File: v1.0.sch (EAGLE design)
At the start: 264 parts, among them J1 DC-044-A, J2 MICROSD-9P, J3 2p-2.54, J4 2p-2.54, J5 16p-2.54, J6 16p-2.54, J8 2p-2.54, Q2 SSM3J328R,LF, Q3 6pF@32.7680kHz, Q4 BSS138W-7-F, Q5 SSM3J328R,LF, SW1 TS-1101F, SW2 TS-1101F, SW3 TS-1101F, SW4 TS-1101F, SW5 TS-1101F, U1 MCP23017-E/SO, U10 74HC139N, U11 BZX84C30, U12 SP483ECN-L, U13 FT232RL-SSOP28, U14 FT232RL-SSOP28, U15 FT232RL-SSOP28, U2 MCP79412-I/SN, U3 LOPY, U4 MAX213IDBR, U5 FT232RL-SSOP28, U6 FT232RL-SSOP28, U7 2x14p-2.54, U8 BR24G32-3, U9 2x14p-2.54, Y2 12MHZ

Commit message: General pendantry of tidying and ERC etc
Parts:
- removed C33: 10uf, Seeed-Capacitor-2016:CERAMIC-10UF-25V-10%-X5R(0805)
- added C26: 10uf, Seeed-Capacitor:TANTALUM-SMD-10UF-16V-10%(AVX-A)
- added D22: RED-0603, Seeed-LED-2016:LED-SMD-RED-DIFFUSED(0603)
- added R4: 220R, Seeed-Resistor:SMD-RES-220R-5%-1/10W(0603)
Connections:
- net LOPY_I2C_5V_PROTECTED renamed N$4
- net PI_I2C_2_5V_P renamed PI_I2C_5V_P2
- net PI_I2C_3V3_10_P renamed PI_I2C_3V3_10
- net PI_I2C_3V3_2_P renamed PI_I2C_3V3_2
- net PI_I2C_3V3_3_P renamed PI_I2C_3V3_1
- net PI_I2C_3V3_4_P renamed PI_I2C_3V3_4
- net PI_I2C_5V_10_P renamed PI_I2C_5V_P9
- net PI_I2C_5V_3_P renamed PI_I2C_5V_P1
- net PI_I2C_5V_4_P renamed PI_I2C_5V_P3
- removed net +3V3_PP: F62.1
- removed net N$18: J2.DATA2
- removed net N$20: J2.DATA1
- removed net N$21: J2.CDN
- removed net PI_I2C_3V3_5_P: F14.2, I2C_6-2.S
- removed net PI_I2C_3V3_6_P: F22.2, I2C_5-2.S
- removed net PI_I2C_3V3_7_P: F16.2, I2C_7-2.S
- removed net PI_I2C_3V3_8_P: F18.2, I2C_8-2.S
- removed net PI_I2C_3V3_9_P: F20.2, I2C_9-2.S
- removed net PI_I2C_5V_5_P: F13.2, I2C_6-1.S
- removed net PI_I2C_5V_6_P: F21.2, I2C_5-1.S
- removed net PI_I2C_5V_7_P: F15.2, I2C_7-1.S
- removed net PI_I2C_5V_8_P: F17.2, I2C_8-1.S
- removed net PI_I2C_5V_9_P: F19.2, I2C_9-1.S
- new net N$5: D22.+, R4.1
- new net PI_I2C_3V3_5: F14.2, I2C_5-2.S
- new net PI_I2C_3V3_6: F16.2, I2C_6-2.S
- new net PI_I2C_3V3_7: F18.2, I2C_7-2.S
- new net PI_I2C_3V3_8: F20.2, I2C_8-2.S
- new net PI_I2C_3V3_9: F22.2, I2C_9-2.S
- new net PI_I2C_5V_P4: F13.2, I2C_5-1.S
- new net PI_I2C_5V_P5: F15.2, I2C_6-1.S
- new net PI_I2C_5V_P6: F17.2, I2C_7-1.S
- new net PI_I2C_5V_P7: F19.2, I2C_8-1.S
- new net PI_I2C_5V_P8: F21.2, I2C_9-1.S
- net +3V3: now also F62.1
- net GND: now also C17.-, C25.1, C26.-, USB1.GND, USB1.SHIELD; no longer C17.+, C33.1
- net LOPY_USB_5V: now also C17.+; no longer C17.-
- net N$105: now also C26.+; no longer C33.2
- net N$83: now also D22.-
- net PI_PWR_CTRL: now also R4.2
- net RXD1: now also U4.ROUT1; no longer U4.DIN1
- net RXD2: now also U4.ROUT2; no longer U4.DIN2
- net RXD3: now also U4.ROUT3; no longer U4.DIN3
- net SHIELD: no longer C25.1, USB1.GND, USB1.SHIELD
- net TXD1: now also U4.DIN1; no longer U4.ROUT1
- net TXD2: now also U4.DIN2; no longer U4.ROUT2
- net TXD3: now also U4.DIN3; no longer U4.ROUT3
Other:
- note added: "Bootloader pins"
- note added: "I2C Sockets"
- note added: "LoPy I2C"
- note added: "LoPy UART"
- note added: "Needs good ground plane for termal issues"
- note added: "RS232"
- note added: "SPI Sockets"
- note added: "TP4 & TP1 should be close together"
- note added: "TTL"
- note added: "crystal tracks should be symetrical"
- note removed: "RPI HUB UART"
- note removed: "RS485 Rpi"
- note removed: "lopy I2C"
- note removed: "lopy SPI"
- note removed: "lopy UART"
- moved on the sheet: BAT1, C13, C17, C19, C20, C23, C25, C28, C30, C32, C34, C35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

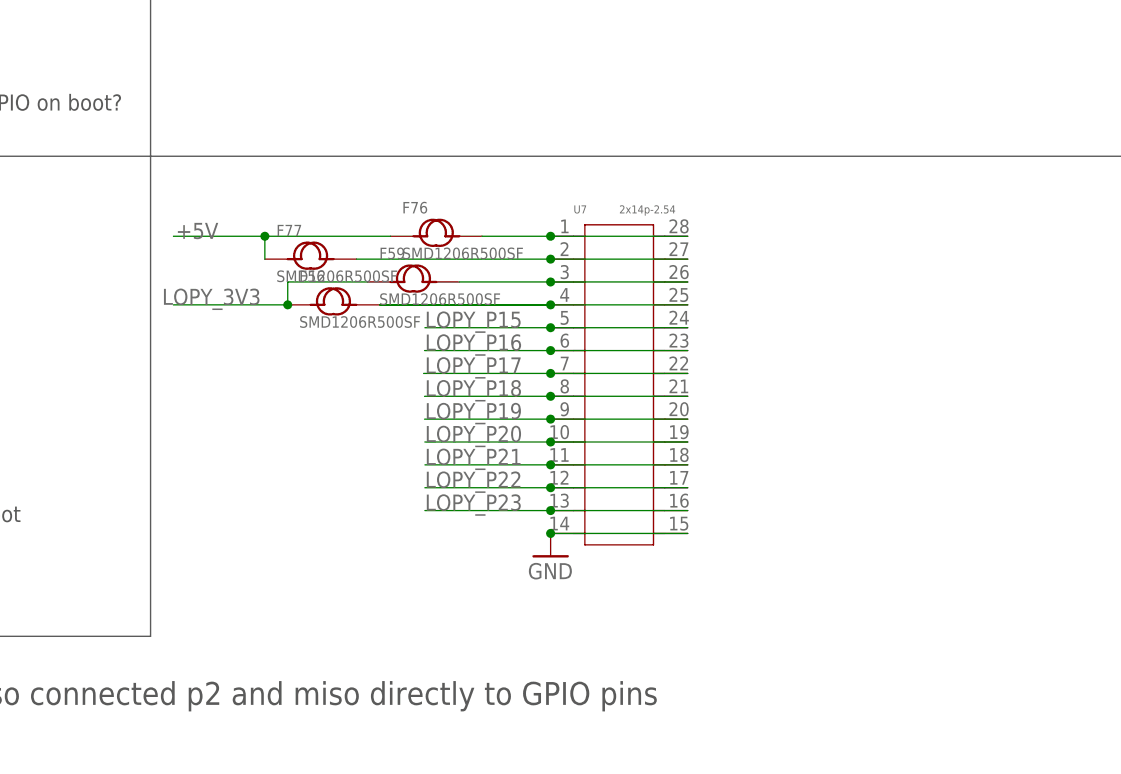
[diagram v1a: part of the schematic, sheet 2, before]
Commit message: Clustering things ready for PCB layout
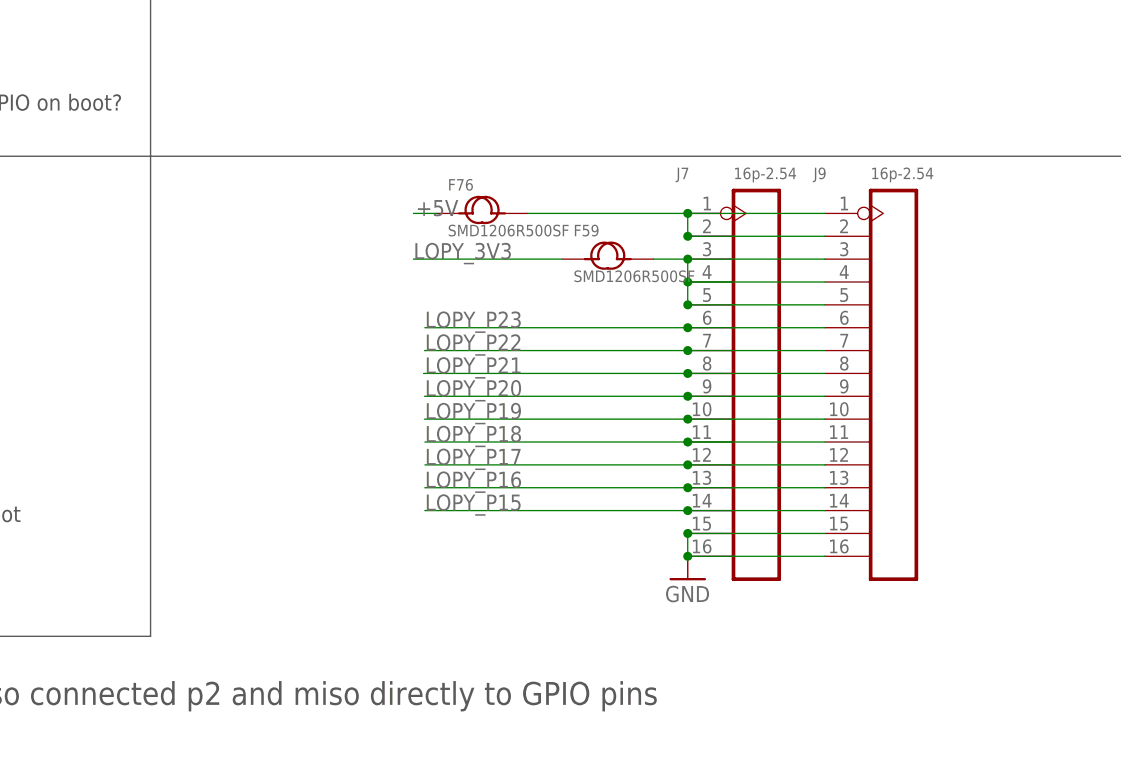
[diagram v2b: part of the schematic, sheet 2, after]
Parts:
- removed F56, F61, F63, F77: SMD1206R500SF, Seeed-Fuse:SMD-PPTC-500MA(1206)
- removed SW4: TS-1101F, Seeed-Switch-2016:DIP-BUTTON(2P-6.0X3.0X4.3MM)-TS-1101F
- removed U7, U9: 2x14p-2.54, Seeed-Connector:DIP-IC-SOCKET(2X14P-2.54)
- added J10, J11, J7, J9: 16p-2.54, Seeed-Connector:DIP-BLACK-MALE-HEADER-VERT(16P-2.54)
- added TP16: TPB2,54, testpad:TPB2,54
- Q1: value 6pF@32.7680kHz -> 32.768khZ@6Pf
- U10: value 74HC139N -> 74HCT139D; device 74HC139N:74HC139N -> imported-parts:74HCT139D
- renumbered Q3 to Q1
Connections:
- net N$12 renamed GPIO_EXP_1
- net N$13 renamed GPIO_EXP_2
- net N$14 renamed GPIO_EXP_3
- net N$15 renamed GPIO_EXP_4
- net N$16 renamed GPIO_EXP_5
- net N$19 renamed GPIO_EXP_6
- net N$22 renamed GPIO_EXP_7
- net N$24 renamed GPIO_EXP_8
- net N$26 renamed GPIO_EXP_9
- net N$27 renamed GPIO_EXP_10
- net N$35 renamed GPIO_EXP_11
- net N$36 renamed GPIO_EXP_12
- net N$37 renamed GPIO_EXP_13
- net N$39 renamed GPIO_EXP_14
- net N$40 renamed GPIO_EXP_15
- net N$8 renamed GPIO_EXP_0
- removed net +5V_PP: F77.2, U7.2, U7.27
- removed net 3V3_PPP: F63.2, U9.25, U9.4
- removed net LOPY_3V3_P: F59.2, U7.26, U7.3
- removed net LOPY_3V3_PP: F56.2, U7.25, U7.4
- removed net N$50: D12.-, SW4.2
- removed net N$83: D10.-, D11.-, D13.-, D14.-, D22.-, D4.-, D5.-, D6.-, D8.-, D9.-, SW1.1
- removed net N$9: F76.2, U7.1, U7.28
- removed net PI_5V_PP: F61.2, U9.2, U9.27
- removed net PI_5V_PROT: F60.2, U9.1, U9.28
- removed net SHIELD: C9.1, USB3.GND, USB3.SHIELD
- new net LED_GND: D10.-, D11.-, D12.-, D13.-, D14.-, D22.-, D4.-, D5.-, D6.-, D8.-, D9.-, SW1.1
- new net LOPY_3V3_FUSED: F59.2, J7.3, J7.4, J7.5, J9.3, J9.4, J9.5
- new net LOPY_5V_FUSED: F76.2, J7.1, J7.2, J9.1, J9.2
- new net N$44: F60.2, J10.1, J10.2, J10.3, J11.1, J11.2, J11.3
- net +3V3: no longer F63.1
- net +3V3_P: now also J10.4, J10.5, J10.6, J11.4, J11.5, J11.6; no longer U9.26, U9.3
- net +5V: no longer F77.1
- net GND: now also C9.1, J10.15, J10.16, J11.15, J11.16, J7.15, J7.16, J9.15, J9.16, USB3.GND, USB3.SHIELD; no longer PI_ADC_1-7.S, PI_ADC_2-7.S, PI_ADC_3-7.S, PI_ADC_4-7.S, SW4.1, U7.14, U7.15, U9.10, U9.14, U9.19
- net GNDA: now also PI_ADC_1-7.S, PI_ADC_2-7.S, PI_ADC_3-7.S, PI_ADC_4-7.S
- net GPIO16_FREE: now also J10.7, J11.7; no longer U9.24, U9.5
- net GPIO18_FREE: now also J10.8, J11.8; no longer U9.23, U9.6
- net GPIO19_FREE: now also J10.9, J11.9; no longer U9.22, U9.7
- net GPIO20_FREE: now also J10.10, J11.10; no longer U9.21, U9.8
- net GPIO21_FREE: now also J10.11, J11.11; no longer U9.20, U9.9
- net GPIO24_FREE: now also J10.12, J11.12; no longer U9.11, U9.18
- net GPIO25_FREE: now also J10.13, J11.13; no longer U9.12, U9.17
- net GPIO26_FREE: now also J10.14, J11.14; no longer U9.13, U9.16
- net LOPY_3V3: no longer F56.1
- net LOPY_P15: now also J7.14, J9.14; no longer U7.24, U7.5
- net LOPY_P16: now also J7.13, J9.13; no longer U7.23, U7.6
- net LOPY_P17: now also J7.12, J9.12; no longer U7.22, U7.7
- net LOPY_P18: now also J7.11, J9.11; no longer U7.21, U7.8
- net LOPY_P19: now also J7.10, J9.10; no longer U7.20, U7.9
- net LOPY_P20: now also J7.9, J9.9; no longer U7.10, U7.19
- net LOPY_P21: now also J7.8, J9.8; no longer U7.11, U7.18
- net LOPY_P22: now also J7.7, J9.7; no longer U7.12, U7.17
- net LOPY_P23: now also J7.6, J9.6; no longer U7.13, U7.16
- net N$80: now also TP16.TP
- net PI_5V: no longer F61.1
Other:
- note added: "Onecall code LFXTAL016178"
- moved on the sheet: D12, F59, F60, F76

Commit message: before autoroute attempt
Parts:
- added H1, H2, H3, H4, H5, H6: MOUNT-HOLE3.0, holes:MOUNT-HOLE3.0
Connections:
- net N$97 renamed EEPROM_WP
- net GND: now also U$4.TAB
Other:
- moved on the sheet: D14
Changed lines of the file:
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@@
 <part name="TP16" library="testpad" library_urn="urn:adsk.eagle:library:385" deviceset="TP" device="B2,54"/>
 <part name="Q1" library="crystal" deviceset="CRYTAL" device="68SMX" value="32.768khZ@6Pf"/>
+<part name="H1" library="holes" library_urn="urn:adsk.eagle:library:237" deviceset="MOUNT-HOLE" device="3.0"/>
+<part name="H2" library="holes" library_urn="urn:adsk.eagle:library:237" deviceset="MOUNT-HOLE" device="3.0"/>
+<part name="H3" library="holes" library_urn="urn:adsk.eagle:library:237" deviceset="MOUNT-HOLE" device="3.0"/>
+<part name="H4" library="holes" library_urn="urn:adsk.eagle:library:237" deviceset="MOUNT-HOLE" device="3.0"/>
+<part name="H5" library="holes" library_urn="urn:adsk.eagle:library:237" deviceset="MOUNT-HOLE" device="3.0"/>
+<part name="H6" library="holes" library_urn="urn:adsk.eagle:library:237" deviceset="MOUNT-HOLE" device="3.0"/>
 </parts>
 <sheets>
@@
 </segment>
 </net>
-<net name="N$97" class="0">
+<net name="EEPROM_WP" class="0">
 <segment>
 <pinref part="U8" gate="G$1" pin="WP"/>
@@
 <wire x1="66.04" y1="99.06" x2="58.42" y2="99.06" width="0.1524" layer="91"/>
 <wire x1="53.34" y1="86.36" x2="58.42" y2="86.36" width="0.1524" layer="91"/>
-<wire x1="58.42" y1="86.36" x2="58.42" y2="99.06" width="0.1524" layer="91"/>
+<wire x1="58.42" y1="86.36" x2="58.42" y2="88.9" width="0.1524" layer="91"/>
 <pinref part="U$4" gate="G$1" pin="ADJ/GND"/>
 <pinref part="C4" gate="G$1" pin="-"/>
+<wire x1="58.42" y1="88.9" x2="58.42" y2="99.06" width="0.1524" layer="91"/>
 <wire x1="53.34" y1="92.71" x2="53.34" y2="86.36" width="0.1524" layer="91"/>
 <junction x="53.34" y="86.36"/>
+<pinref part="U$4" gate="G$1" pin="TAB"/>
+<wire x1="86.36" y1="88.9" x2="58.42" y2="88.9" width="0.1524" layer="91"/>
+<junction x="58.42" y="88.9"/>
 </segment>
 <segment>
@@
 <instance part="D10" gate="G$1" x="33.02" y="129.54" rot="R270"/>
 <instance part="R11" gate="G$1" x="33.02" y="142.24" rot="R90"/>
-<instance part="D14" gate="G$1" x="20.32" y="129.54" rot="R270"/>
+<instance part="D14" gate="G$1" x="20.32" y="130.81" rot="R270"/>
 <instance part="R22" gate="G$1" x="20.32" y="142.24" rot="R90"/>
 <instance part="R35" gate="G$1" x="5.08" y="142.24" rot="R90"/>
@@
 <instance part="D22" gate="G$1" x="137.16" y="129.54" rot="R270"/>
 <instance part="R4" gate="G$1" x="137.16" y="140.97" rot="R90"/>
+<instance part="H1" gate="G$1" x="322.58" y="149.86"/>
+<instance part="H2" gate="G$1" x="322.58" y="143.51"/>
+<instance part="H3" gate="G$1" x="322.58" y="137.16"/>
+<instance part="H4" gate="G$1" x="322.58" y="129.54"/>
+<instance part="H5" gate="G$1" x="322.58" y="123.19"/>
+<instance part="H6" gate="G$1" x="322.58" y="115.57"/>
 </instances>
 <busses>
@@
 <pinref part="D14" gate="G$1" pin="+"/>
 <pinref part="R22" gate="G$1" pin="1"/>
-<wire x1="20.32" y1="133.35" x2="20.32" y2="138.43" width="0.1524" layer="91"/>
+<wire x1="20.32" y1="134.62" x2="20.32" y2="138.43" width="0.1524" layer="91"/>
 </segment>
 </net>
@@
 <segment>
 <pinref part="D14" gate="G$1" pin="-"/>
-<wire x1="20.32" y1="125.73" x2="20.32" y2="121.92" width="0.1524" layer="91"/>
+<wire x1="20.32" y1="127" x2="20.32" y2="121.92" width="0.1524" layer="91"/>
 <pinref part="D10" gate="G$1" pin="-"/>
 <wire x1="33.02" y1="125.73" x2="33.02" y2="121.92" width="0.1524" layer="91"/>
@@
 <wire x1="124.46" y1="121.92" x2="137.16" y2="121.92" width="0.1524" layer="91"/>
 <junction x="124.46" y="121.92"/>
-</segment>
-</net>
+<label x="7.62" y="121.92" size="1.778" layer="95"/>
+</segment>
+</net>

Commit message: Most of the board laid out
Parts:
- added TP17: TPB2,54, testpad:TPB2,54
- C5, C8: value 1UF 6.3V -> 10uf; device Seeed-Capacitor-2016:CERAMIC-1UF-6.3V-10%-X5R(0402) -> Seeed-Capacitor:TANTALUM-SMD-10UF-10V-10%(AVX-A)
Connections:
- net +3V3_P renamed GPIO_3V3_FUSED
- net FTID2_CBUS2 renamed RS485_CBUS2
- net N$10 renamed RS485_CBUS0
- net N$109 renamed RS232_1_LED1
- net N$110 renamed RS232_1_LED2
- net N$113 renamed RS232_2_LED1
- net N$114 renamed RS232_2_LED2
- net N$117 renamed RS232_3_LED1
- net N$118 renamed RS232_3_LED2
- net N$43 renamed USB_HUB_DRV
- net N$44 renamed GPIO_5V_FUSED
- removed net 3V3_SMOOTH: C14.2, F39.1, F41.1, F43.1, F45.1, L2.2, R10.2, R16.2, TP3.TP, U$7.VDD
- removed net N$48: R25.1, SW3.2
- new net N$9: R25.1, SW3.1
- net +3V3: now also R16.2, U$7.VDD
- net +3V3_SMOOTH: now also C14.2, C5.+, C8.+, F39.1, F41.1, F43.1, F45.1, L2.2, R10.2, TP3.TP; no longer C5.1, C8.1
- net 5V_USB_HUB: no longer C32.1, U$6.VDD5
- net 5V_USB_HUB_FERRITE: now also C32.1, U$6.VDD5
- net GNDA: now also C5.-, C8.-; no longer C5.2, C8.2
- net GPIO18_FREE: now also PCB1.GPIO18
- net RS485_A: now also SW3.2; no longer SW3.1
- net RTC_BATT: now also TP17.TP
- net USB3_DM: now also U$6.DM4; no longer U$6.DM3
- net USB3_DP: now also U$6.DP4; no longer U$6.DP3
- net USB4_DM: now also U$6.DM3; no longer U$6.DM4
- net USB4_DP: now also U$6.DP3; no longer U$6.DP4
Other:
- moved on the sheet: SW3

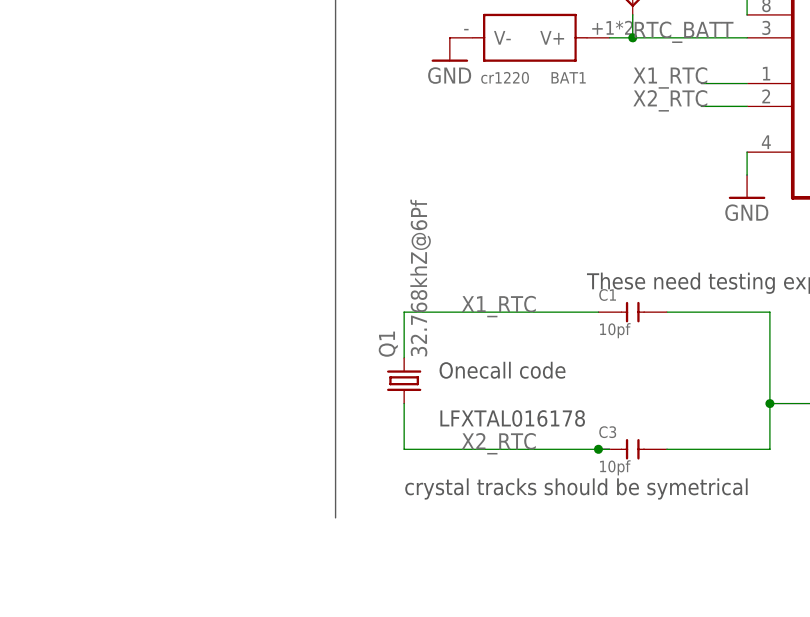
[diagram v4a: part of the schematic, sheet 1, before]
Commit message: Board layout potentially complete - just needs a name now
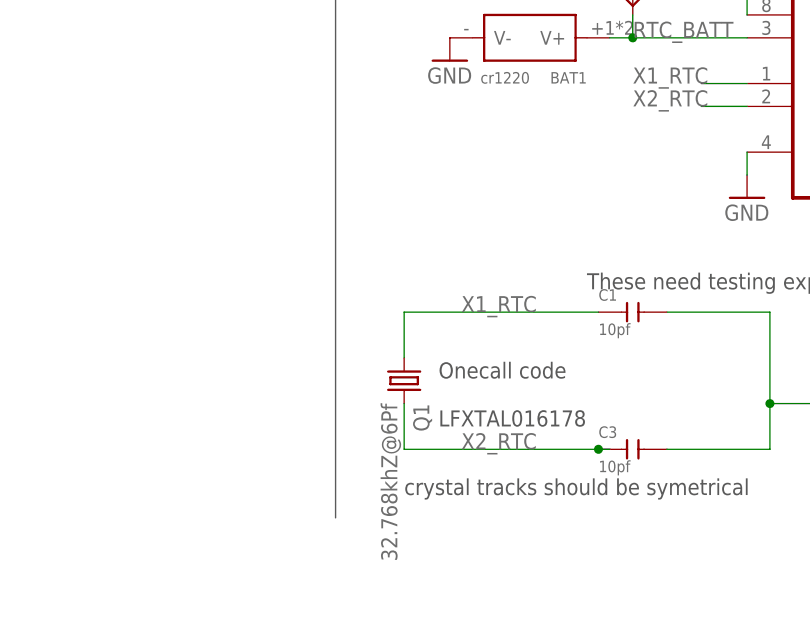
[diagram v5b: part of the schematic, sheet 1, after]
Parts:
- Q1: device crystal:CRYTAL68SMX -> imported-parts:LFXTAL016178
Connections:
- net X1_RTC: now also Q1.1; no longer Q1.2
- net X2_RTC: now also Q1.2; no longer Q1.1
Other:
- moved on the sheet: Q1
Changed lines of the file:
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@@
 <part name="J11" library="Seeed-Connector" library_urn="urn:adsk.eagle:library:465" deviceset="DIP-BLACK-MALE-HEADER-VERT(16P-2.54)" device="" value="16p-2.54"/>
 <part name="TP16" library="testpad" library_urn="urn:adsk.eagle:library:385" deviceset="TP" device="B2,54"/>
-<part name="Q1" library="crystal" deviceset="CRYTAL" device="68SMX" value="32.768khZ@6Pf"/>
+<part name="Q1" library="imported-parts" deviceset="LFXTAL016178" device="" value="32.768khZ@6Pf"/>
 <part name="H1" library="holes" library_urn="urn:adsk.eagle:library:237" deviceset="MOUNT-HOLE" device="3.0"/>
 <part name="H2" library="holes" library_urn="urn:adsk.eagle:library:237" deviceset="MOUNT-HOLE" device="3.0"/>
@@
 <instance part="J10" gate="G$1" x="355.6" y="48.26"/>
 <instance part="J11" gate="G$1" x="369.57" y="48.26"/>
-<instance part="Q1" gate="G$1" x="167.64" y="17.78" rot="R90"/>
+<instance part="Q1" gate="G$1" x="167.64" y="17.78" rot="R270"/>
 <instance part="TP17" gate="G$1" x="193.04" y="60.96"/>
 </instances>
@@
 </segment>
 <segment>
-<wire x1="167.64" y1="20.32" x2="167.64" y2="25.4" width="0.1524" layer="91"/>
 <label x="173.99" y="25.4" size="1.778" layer="95"/>
 <wire x1="167.64" y1="25.4" x2="189.23" y2="25.4" width="0.1524" layer="91"/>
 <pinref part="C1" gate="G$1" pin="1"/>
-<pinref part="Q1" gate="G$1" pin="2"/>
+<pinref part="Q1" gate="G$1" pin="1"/>
+<wire x1="167.64" y1="25.4" x2="167.64" y2="20.32" width="0.1524" layer="91"/>
 </segment>
 </net>
@@
 </segment>
 <segment>
-<wire x1="167.64" y1="15.24" x2="167.64" y2="10.16" width="0.1524" layer="91"/>
 <wire x1="167.64" y1="10.16" x2="189.23" y2="10.16" width="0.1524" layer="91"/>
 <pinref part="C3" gate="G$1" pin="1"/>
@@
 <junction x="189.23" y="10.16"/>
 <label x="173.99" y="10.16" size="1.778" layer="95"/>
-<pinref part="Q1" gate="G$1" pin="1"/>
-</segment>
-</net>
+<pinref part="Q1" gate="G$1" pin="2"/>
+<wire x1="167.64" y1="10.16" x2="167.64" y2="15.24" width="0.1524" layer="91"/>
+</segment>
+</net>
